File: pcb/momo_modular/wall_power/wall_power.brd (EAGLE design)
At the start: 7 x 7.1 mm, 23 parts

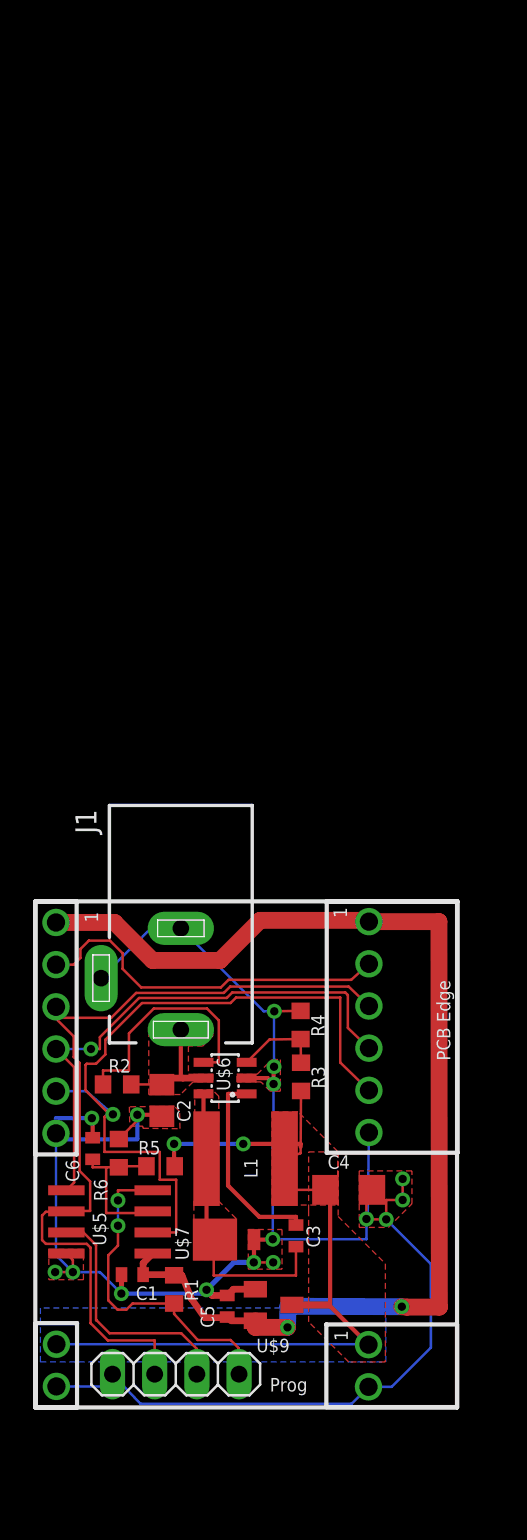
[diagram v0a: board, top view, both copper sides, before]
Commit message: Laid out version 2 of the controller board and wall power board with better power supply layout to minimize noise coupling. Created version 1 of the gsm board. Changed Momo edge connector to an 8 pin version.
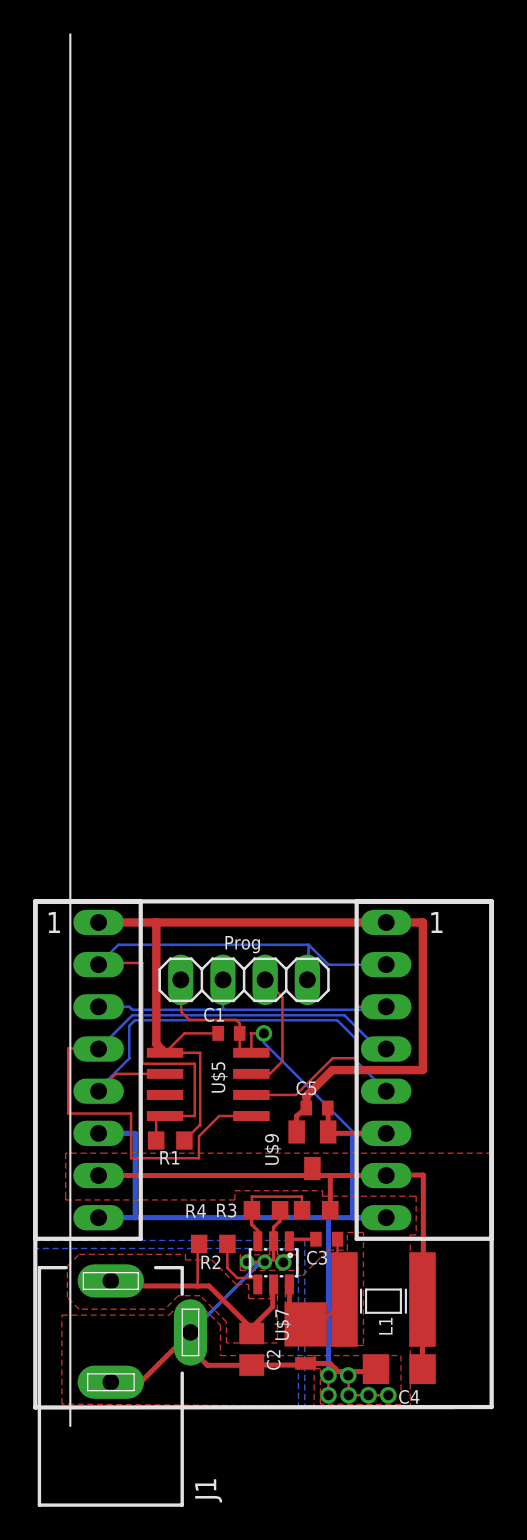
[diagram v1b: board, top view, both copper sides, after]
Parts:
- removed C6: 100 nF, rcl:C0402
- removed R5, R6: 500K, rcl:R0603
- removed U$3: MOMO-EDGE-POWER-M, components:MOMO-EDGE-SMALL-2M
- removed U$4: MOMO-EDGE-POWER-F, components:MOMO-EDGE-SMALL-2F
- U$1: value MOMO-EDGE-SMALL-M -> MOMO-EDGE-8F; device components:MOMO-EDGE-SMALL-6M -> components:MOMO-EDGE-8F
- U$2: value MOMO-EDGE-SMALL-F -> MOMO-EDGE-8M; device components:MOMO-EDGE-SMALL-6F -> components:MOMO-EDGE-8M
- moved JP1 24.1 mm to (12.6, 25.8)
- moved J1 21.7 mm to (4.55, 4.52), turned to 0 degrees
- moved U$1 20.2 mm to (21.1, 19.1), turned to 0 degrees
- moved U$2 16.7 mm to (3.81, 19.1), turned to 0 degrees
- moved C2 15.9 mm to (13.0, 3.51)
- moved C1 15.6 mm to (11.7, 22.5), turned to 0 degrees
- moved C5 13.1 mm to (17.0, 18.0), turned to 0 degrees
- moved U$8 11.9 mm to (18.6, 6.50)
- moved U$6 11.5 mm to (14.4, 8.71), turned to 180 degrees
- moved R4 11.3 mm to (13.9, 11.9), turned to 180 degrees
- moved C4 11.2 mm to (21.9, 2.31), turned to 180 degrees
- moved R2 11.2 mm to (10.7, 9.86), turned to 0 degrees
- moved U$5 10.2 mm to (10.4, 19.5), turned to 270 degrees
- moved U$9 9.61 mm to (16.7, 15.5), turned to 180 degrees
- moved R1 8.97 mm to (8.13, 16.1), turned to 180 degrees
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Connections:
- removed net N$5: C6.1, R5.1, R6.2, U$5.3
- removed net NC: U$1.2, U$2.2
- net CLK: now also U$1.CLK, U$2.CLK; no longer U$1.3, U$2.3
- net DAT: now also U$1.DAT, U$2.DAT; no longer U$1.4, U$2.4
- net GND: now also U$1.GND, U$1.PGND, U$2.GND, U$2.PGND; no longer C6.2, R6.1, U$1.6, U$2.6, U$3.2, U$4.2
- net IRQ: now also U$1.ARLM, U$2.ALRM; no longer U$1.5, U$2.5
- net N$1: now also U$1.NV, U$2.NC
- net V+: now also U$1.V4., U$2.V4; no longer R5.2, U$3.1, U$4.1
- net VCCINT: now also U$1.V28, U$2.V28; no longer U$1.1, U$2.1
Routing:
- net GND: track 129.5 -> 103.0 mm, vias 16 -> 10
- net NC: track 22.0 -> 0.00 mm
- net CLK: track 51.7 -> 31.4 mm
- net N$1: track 20.5 -> 39.4 mm, vias 2 -> 0
- net IRQ: track 44.9 -> 27.3 mm, vias 1 -> 0
- net V+: track 49.8 -> 33.8 mm, vias 2 -> 0
- net VCCINT: track 70.9 -> 58.3 mm, vias 2 -> 0
- net N$3: track 14.4 -> 3.93 mm
- net N$4: track 12.0 -> 1.65 mm
- net N$5: track 9.44 -> 0.00 mm
- net N$2: track 18.1 -> 9.58 mm
- net +12V: track 7.81 -> 15.8 mm
- net DAT: track 32.4 -> 40.3 mm, vias 1 -> 0
- net N$8: track 14.9 -> 7.52 mm
- net N$6: track 5.24 -> 6.68 mm
- removed copper zone on layer 16, net V+
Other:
- outline, holes or cut-outs redrawn

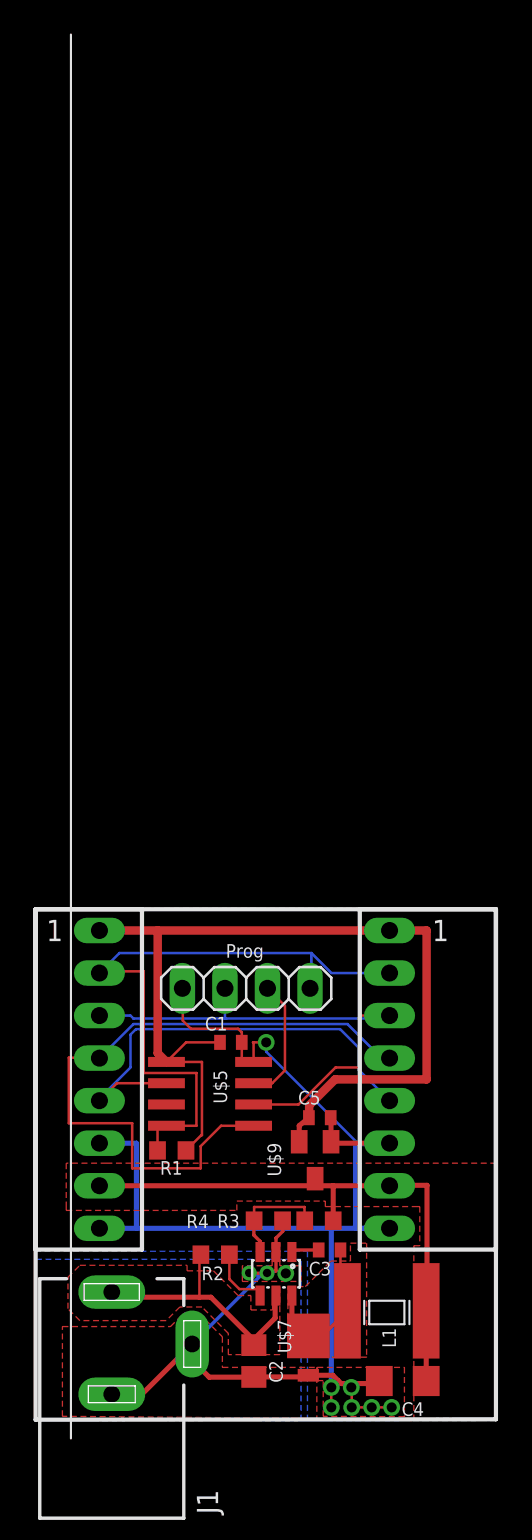
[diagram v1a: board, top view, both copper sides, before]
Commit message: Updated layout of wall power board slightly and added outline layer.
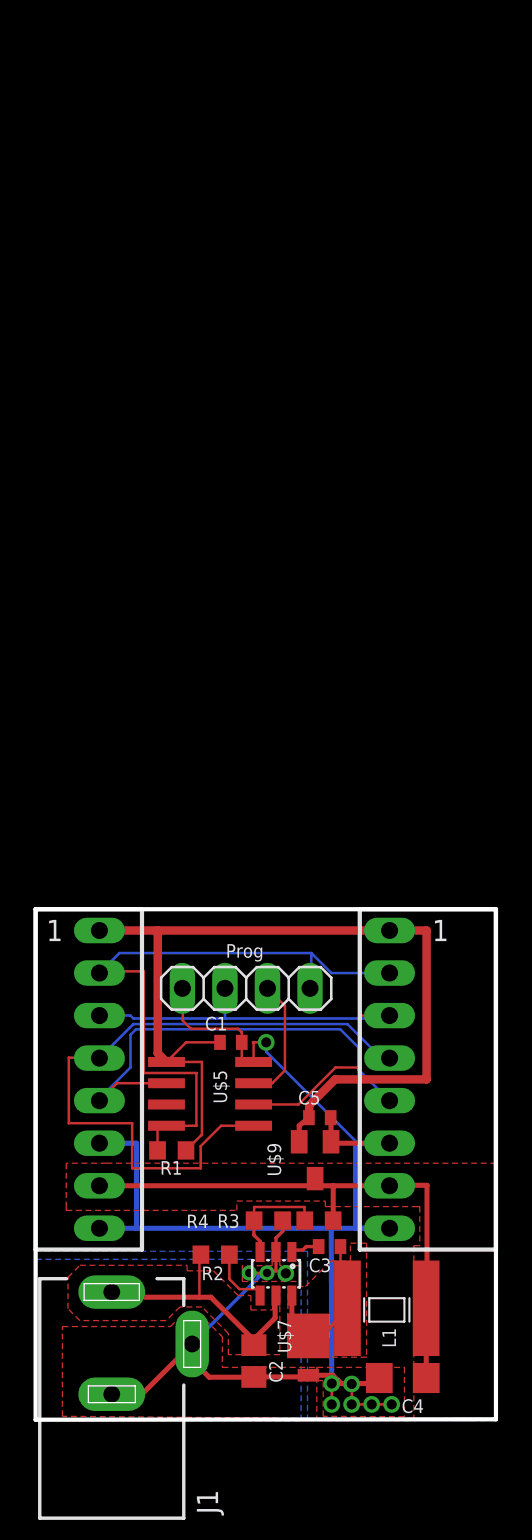
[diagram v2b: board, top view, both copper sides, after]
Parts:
- moved C3 0.20 mm to (17.6, 10.3)
- moved C4 0.18 mm to (21.9, 2.49)
- moved U$8 0.15 mm to (18.6, 6.65)
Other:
- board size 7 x 7.1 mm -> 27.5 x 30.5 mm
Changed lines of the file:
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@@
 <board>
 <plain>
-<wire x1="0" y1="0" x2="27.4828" y2="0.0254" width="0.254" layer="21"/>
-<wire x1="27.4828" y1="30.48" x2="0" y2="30.48" width="0.254" layer="21"/>
-<wire x1="0" y1="30.48" x2="0" y2="0" width="0.254" layer="21"/>
+<wire x1="0" y1="0" x2="27.4828" y2="0.0254" width="0.254" layer="20"/>
+<wire x1="27.4828" y1="30.48" x2="0" y2="30.48" width="0.254" layer="20"/>
+<wire x1="0" y1="30.48" x2="0" y2="0" width="0.254" layer="20"/>
 <text x="21.5138" y="4.2926" size="0.8128" layer="21" rot="R90">L1</text>
 <text x="11.3538" y="27.5844" size="0.8128" layer="21">Prog</text>
-<wire x1="27.4828" y1="30.48" x2="27.4828" y2="0.0254" width="0.254" layer="21"/>
+<wire x1="27.4828" y1="30.48" x2="27.4828" y2="0.0254" width="0.254" layer="20"/>
+<dimension x1="0" y1="0" x2="-0.0508" y2="30.5308" x3="-2.0574" y3="15.2654" textsize="1.778" layer="49" dtype="vertical" unit="inch" precision="3" visible="yes"/>
+<dimension x1="0" y1="30.48" x2="27.5336" y2="27.9908" x3="13.7668" y3="32.4104" textsize="1.778" layer="49" dtype="horizontal" unit="inch" precision="3" visible="yes"/>
 </plain>
 <attributes>
@@
 <param name="mdViaViaSameLayer" value="8mil"/>
 <param name="mnLayersViaInSmd" value="2"/>
-<param name="mdCopperDimension" value="40mil"/>
+<param name="mdCopperDimension" value="10mil"/>
 <param name="mdDrill" value="8mil"/>
 <param name="mdSmdStop" value="0mil"/>
@@
 <attribute name="NAME" x="15.2654" y="3.9751" size="0.8128" layer="25" rot="R90"/>
 </element>
-<element name="C3" library="rcl" package="C0402" value="10 nF" x="17.5514" y="10.1346" smashed="yes">
-<attribute name="NAME" x="16.3068" y="8.6106" size="0.8128" layer="25"/>
-<attribute name="VALUE" x="16.9164" y="8.2296" size="1.27" layer="27"/>
-</element>
-<element name="U$8" library="components" package="NR6028-INDUCTOR" value="4.7 uH" x="18.6182" y="6.5024" smashed="yes"/>
-<element name="C4" library="rcl" package="C1206" value="22 uF" x="21.9202" y="2.3114" smashed="yes" rot="R180">
-<attribute name="NAME" x="23.1902" y="1.0414" size="0.8128" layer="25" rot="R180"/>
-<attribute name="VALUE" x="23.1902" y="4.8514" size="1.27" layer="27" rot="R180"/>
+<element name="C3" library="rcl" package="C0402" value="10 nF" x="17.5514" y="10.3378" smashed="yes">
+<attribute name="NAME" x="16.3068" y="8.8138" size="0.8128" layer="25"/>
+<attribute name="VALUE" x="16.9164" y="8.4328" size="1.27" layer="27"/>
+</element>
+<element name="U$8" library="components" package="NR6028-INDUCTOR" value="4.7 uH" x="18.6182" y="6.6548" smashed="yes"/>
+<element name="C4" library="rcl" package="C1206" value="22 uF" x="21.9202" y="2.4892" smashed="yes" rot="R180">
+<attribute name="NAME" x="23.1902" y="1.2192" size="0.8128" layer="25" rot="R180"/>
+<attribute name="VALUE" x="23.1902" y="5.0292" size="1.27" layer="27" rot="R180"/>
 </element>
 <element name="R3" library="rcl" package="R0603" value="50K 1%" x="16.9164" y="11.8872" smashed="yes">
@@
 <wire x1="18.2372" y1="2.159" x2="18.288" y2="2.159" width="0.3048" layer="1"/>
 <wire x1="18.288" y1="2.159" x2="20.4186" y2="2.159" width="0.3048" layer="1"/>
-<wire x1="20.4186" y1="2.159" x2="20.5202" y2="2.3114" width="0.3048" layer="1"/>
+<wire x1="20.4186" y1="2.159" x2="20.5202" y2="2.4892" width="0.3048" layer="1"/>
 <wire x1="14.351" y1="10.0122" x2="14.351" y2="10.8458" width="0.2032" layer="1"/>
 <wire x1="14.351" y1="10.8458" x2="14.7574" y2="11.2522" width="0.2032" layer="1"/>
@@
 <vertex x="14.5796" y="10.5664"/>
 </polygon>
-<via x="18.8468" y="1.9304" extent="1-16" drill="0.6"/>
-<via x="17.653" y="1.9304" extent="1-16" drill="0.6"/>
-<via x="17.653" y="0.7366" extent="1-16" drill="0.6"/>
-<via x="18.8722" y="0.7366" extent="1-16" drill="0.6"/>
-<via x="20.066" y="0.7366" extent="1-16" drill="0.6"/>
-<via x="21.2598" y="0.7366" extent="1-16" drill="0.6"/>
-<wire x1="21.2598" y1="0.7366" x2="20.066" y2="0.7366" width="0.1524" layer="1"/>
-<wire x1="20.066" y1="0.7366" x2="18.8722" y2="0.7366" width="0.1524" layer="1"/>
-<wire x1="18.8722" y1="0.7366" x2="18.8722" y2="1.905" width="0.1524" layer="1"/>
-<wire x1="18.8722" y1="1.905" x2="18.8468" y2="1.9304" width="0.1524" layer="1"/>
-<wire x1="17.653" y1="0.7366" x2="17.653" y2="1.9304" width="0.1524" layer="1"/>
-<wire x1="17.653" y1="1.9304" x2="17.653" y2="1.9558" width="0.1524" layer="1"/>
+<via x="18.8722" y="2.1336" extent="1-16" drill="0.6"/>
+<via x="17.6784" y="2.159" extent="1-16" drill="0.6"/>
+<via x="17.6784" y="0.9144" extent="1-16" drill="0.6"/>
+<via x="18.8722" y="0.9144" extent="1-16" drill="0.6"/>
+<via x="20.066" y="0.9144" extent="1-16" drill="0.6"/>
+<via x="21.2598" y="0.9144" extent="1-16" drill="0.6"/>
+<wire x1="21.2598" y1="0.9144" x2="20.066" y2="0.9144" width="0.1524" layer="1"/>
+<wire x1="20.066" y1="0.9144" x2="18.8722" y2="0.9144" width="0.1524" layer="1"/>
+<wire x1="18.8722" y1="0.9144" x2="18.8722" y2="2.1336" width="0.1524" layer="1"/>
+<wire x1="17.6784" y1="0.9144" x2="17.6784" y2="2.159" width="0.1524" layer="1"/>
+<wire x1="17.6784" y1="2.159" x2="17.653" y2="1.9558" width="0.1524" layer="1"/>
 <wire x1="17.653" y1="1.9558" x2="18.0467" y2="2.3495" width="0.1524" layer="1"/>
-<wire x1="18.8468" y1="1.9304" x2="18.5166" y2="1.9304" width="0.1524" layer="1"/>
+<wire x1="18.8722" y1="2.1336" x2="18.5166" y2="1.9304" width="0.1524" layer="1"/>
 <wire x1="18.5166" y1="1.9304" x2="18.288" y2="2.159" width="0.1524" layer="1"/>
 <polygon width="0.1524" layer="16" thermals="no">
@@
 <wire x1="3.81" y1="11.43" x2="6.0198" y2="11.43" width="0.3048" layer="16"/>
 <wire x1="6.0198" y1="11.43" x2="17.653" y2="11.43" width="0.3048" layer="16"/>
-<wire x1="17.653" y1="11.43" x2="17.653" y2="1.9304" width="0.3048" layer="16"/>
+<wire x1="17.653" y1="11.43" x2="17.6784" y2="2.159" width="0.3048" layer="16"/>
 <wire x1="21.1328" y1="11.43" x2="17.653" y2="11.43" width="0.3048" layer="16"/>
 <wire x1="21.1328" y1="11.43" x2="19.1008" y2="11.43" width="0.3048" layer="16"/>
@@
 <contactref element="C3" pad="1"/>
 <wire x1="15.301" y1="10.0122" x2="15.4234" y2="10.1346" width="0.2032" layer="1"/>
-<wire x1="15.4234" y1="10.1346" x2="16.9014" y2="10.1346" width="0.2032" layer="1"/>
+<wire x1="15.4234" y1="10.1346" x2="15.9512" y2="10.1346" width="0.2032" layer="1"/>
+<wire x1="15.9512" y1="10.1346" x2="16.1544" y2="10.3378" width="0.2032" layer="1"/>
+<wire x1="16.1544" y1="10.3378" x2="16.9014" y2="10.3378" width="0.2032" layer="1"/>
 </signal>
 <signal name="N$2">
@@
 <wire x1="15.301" y1="5.9842" x2="16.2814" y2="5.0038" width="0.3048" layer="1"/>
 <wire x1="16.2814" y1="5.0038" x2="17.1196" y2="5.0038" width="0.2032" layer="1"/>
-<wire x1="17.1196" y1="5.0038" x2="18.6182" y2="6.5024" width="0.2032" layer="1"/>
+<wire x1="17.1196" y1="5.0038" x2="18.6182" y2="6.6548" width="0.2032" layer="1"/>
 <polygon width="0.1524" layer="1" thermals="no">
 <vertex x="15.0622" y="7.9502"/>
@@
 <vertex x="15.0622" y="3.7338"/>
 </polygon>
-<wire x1="18.2014" y1="10.1346" x2="18.2014" y2="8.9512" width="0.1524" layer="1"/>
+<wire x1="18.2014" y1="10.3378" x2="18.2014" y2="8.9512" width="0.1524" layer="1"/>
 <wire x1="18.2014" y1="8.9512" x2="18.2118" y2="8.9408" width="0.1524" layer="1"/>
 <wire x1="18.2118" y1="8.9408" x2="18.2118" y2="6.9088" width="0.1524" layer="1"/>
-<wire x1="18.2118" y1="6.9088" x2="18.6182" y2="6.5024" width="0.1524" layer="1"/>
+<wire x1="18.2118" y1="6.9088" x2="18.6182" y2="6.6548" width="0.1524" layer="1"/>
 </signal>
 <signal name="N$6">
@@
 <contactref element="U$1" pad="V4."/>
 <contactref element="U$2" pad="V4"/>
-<wire x1="23.3182" y1="6.5024" x2="23.3202" y2="6.5024" width="0.3048" layer="1"/>
-<wire x1="23.3202" y1="6.5024" x2="23.3202" y2="2.3114" width="0.3048" layer="1"/>
-<wire x1="23.3182" y1="6.5024" x2="23.368" y2="6.5024" width="0.3048" layer="1"/>
+<wire x1="23.3182" y1="6.6548" x2="23.3202" y2="6.5024" width="0.3048" layer="1"/>
+<wire x1="23.3202" y1="6.5024" x2="23.3202" y2="2.4892" width="0.3048" layer="1"/>
+<wire x1="23.3182" y1="6.6548" x2="23.368" y2="6.5024" width="0.3048" layer="1"/>
 <wire x1="23.368" y1="6.5024" x2="23.368" y2="13.9954" width="0.3048" layer="1"/>
 <wire x1="23.368" y1="13.9954" x2="21.1328" y2="13.9954" width="0.3048" layer="1"/>
